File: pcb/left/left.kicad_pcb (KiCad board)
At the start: 2 copper layers, 35.6 x 58.4 mm, 21 parts

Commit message: improve basic design
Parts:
- moved LED3 20.8 mm to (15.2, 27.9), turned to 0 degrees
- moved THUMB1 17.6 mm to (16.5, 66.0)
- moved REF** 15.5 mm to (25.4, 66.0)
- moved REF** 15.2 mm to (0.00, 66.0)
- moved PullR1 14.2 mm to (5.08, 53.3)
- moved PullR2 14.2 mm to (8.89, 53.3)
- moved PullR3 14.0 mm to (12.7, 41.9)
- moved LED2 13.7 mm to (10.2, 27.9), turned to 0 degrees
- moved LEDR3 13.7 mm to (15.2, 31.8)
- moved RST_SW1 13.0 mm to (26.7, 36.1)
- moved RJ45 13.0 mm to (15.2, 55.9)
- moved SIDE1 10.2 mm to (16.5, 61.0)
- moved LEDR2 7.41 mm to (10.2, 31.8), turned to 270 degrees
- moved LED1 6.84 mm to (5.08, 27.9), turned to 0 degrees
- moved REF** 2.54 mm to (25.4, 0.00)
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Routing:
- net GND: track 0.00 -> 21.7 mm
- net +5V: track 0.00 -> 2.54 mm
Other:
- board size 35.6 x 58.4 mm -> 33 x 73.7 mm

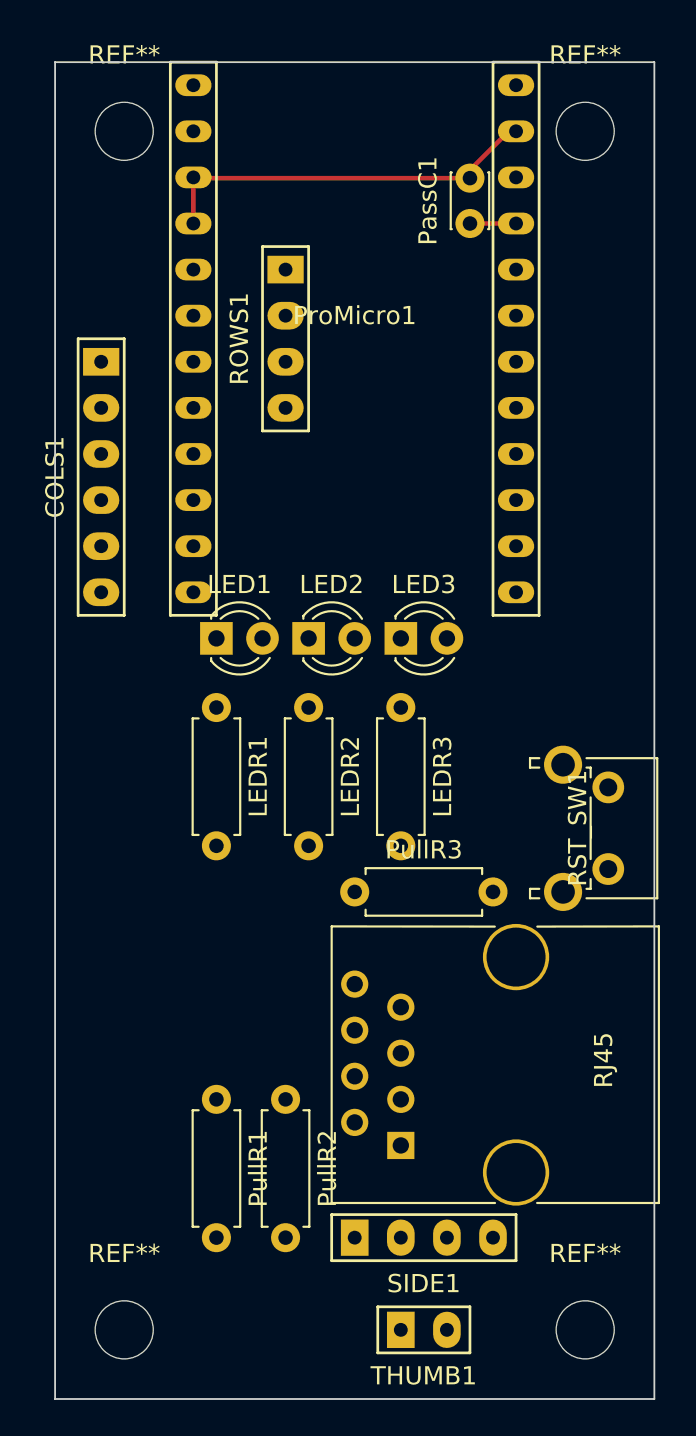
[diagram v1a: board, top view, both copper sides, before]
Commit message: resize pcb shorten pcb length a bit.
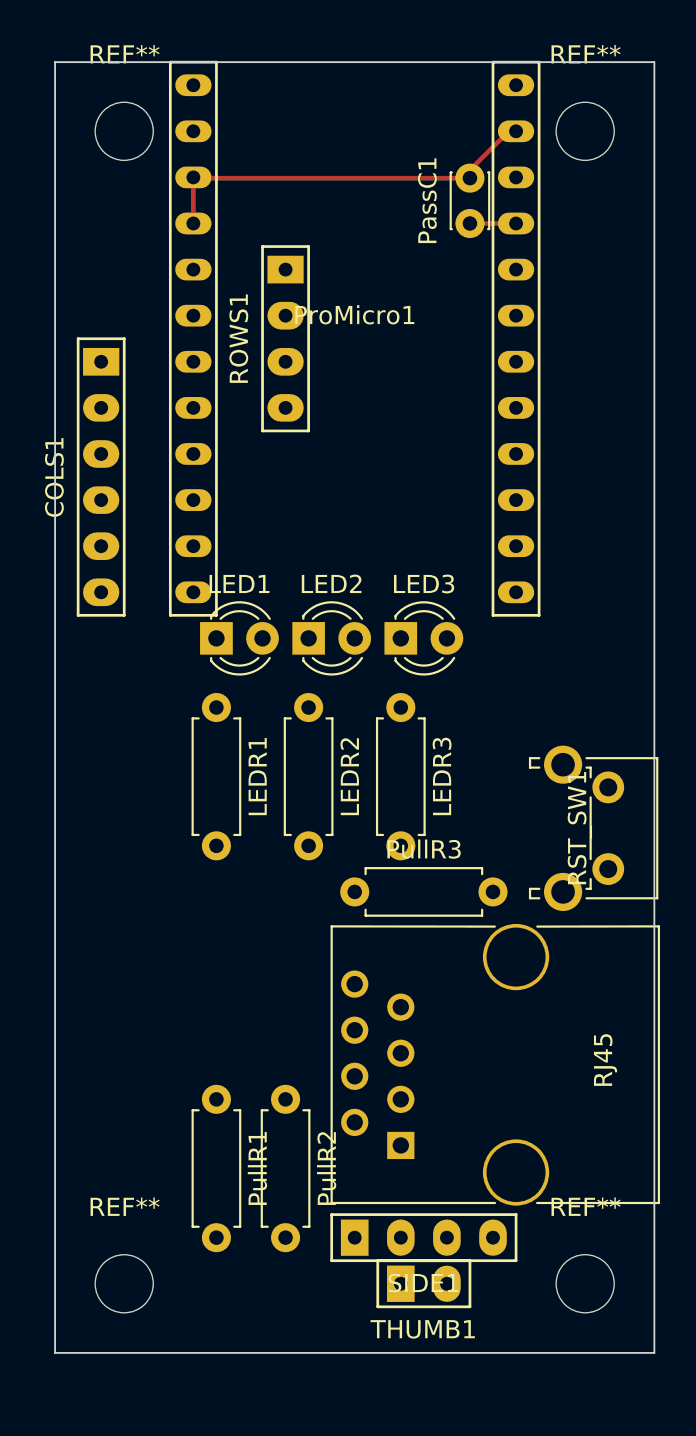
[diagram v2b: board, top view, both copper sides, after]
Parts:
- moved REF** 2.54 mm to (0.00, 63.5)
- moved REF** 2.54 mm to (25.4, 63.5)
- moved THUMB1 2.54 mm to (16.5, 63.5)
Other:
- board size 33 x 73.7 mm -> 33 x 71.1 mm
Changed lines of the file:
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@@
   (general
     (links 45)
-    (no_connects 45)
-    (area -8.290143 -5.178 36.230143 56.958)
+    (no_connects 41)
+    (area -9.560143 -5.178 34.960143 72.198)
     (thickness 1.6)
     (drawings 4)
@@
   )
   (module 4x6t2:Wirepad_01x02 (layer F.Cu)
-    (at 16.51 66.04 90)
+    (at 16.51 63.5 90)
     (fp_text reference THUMB1 (at -2.54 0 180) (layer F.SilkS)
       (effects (font (size 1 1) (thickness 0.15)))
@@
   )
   (module Mounting_Holes:MountingHole_3.2mm_M3 (layer F.Cu)
-    (at 0 66.04)
+    (at 0 63.5)
     (descr "Mounting Hole 3.2mm, no annular, M3")
     (tags "mounting hole 3.2mm no annular m3")
@@
   )
   (module Mounting_Holes:MountingHole_3.2mm_M3 (layer F.Cu)
-    (at 25.4 66.04)
+    (at 25.4 63.5)
     (descr "Mounting Hole 3.2mm, no annular, M3")
     (tags "mounting hole 3.2mm no annular m3")
@@
     (pad 1 np_thru_hole circle (at 0 0) (size 3.2 3.2) (drill 3.2) (layers *.Cu *.Mask))
   )
-  (gr_line (start -3.81 69.85) (end -3.81 -3.81) (layer Edge.Cuts) (width 0.1))
-  (gr_line (start 29.21 69.85) (end -3.81 69.85) (layer Edge.Cuts) (width 0.1))
-  (gr_line (start 29.21 -3.81) (end 29.21 69.85) (layer Edge.Cuts) (width 0.1))
+  (gr_line (start -3.81 67.31) (end -3.81 -3.81) (layer Edge.Cuts) (width 0.1))
+  (gr_line (start 29.21 67.31) (end -3.81 67.31) (layer Edge.Cuts) (width 0.1))
+  (gr_line (start 29.21 -3.81) (end 29.21 67.31) (layer Edge.Cuts) (width 0.1))
   (gr_line (start -3.81 -3.81) (end 29.21 -3.81) (layer Edge.Cuts) (width 0.1))
   (segment (start 3.81 5.08) (end 3.81 2.54) (width 0.25) (layer F.Cu) (net 13))

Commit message: wiring left
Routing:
- net GND: track 21.7 -> 130.2 mm
- net /RST: track 0.00 -> 66.7 mm, vias 0 -> 2
- net +5V: track 2.54 -> 65.7 mm, vias 0 -> 2
- net /SDA: track 0.00 -> 59.5 mm
- net /X: track 0.00 -> 54.8 mm
- net /SCL: track 0.00 -> 51.3 mm
- net /Y: track 0.00 -> 49.8 mm
- net /Thumb_key: track 0.00 -> 40.7 mm, vias 0 -> 1
- net /LED1: track 0.00 -> 18.2 mm
- net /COL0: track 0.00 -> 17.6 mm
- net /COL1: track 0.00 -> 17.5 mm
- net /ROW3: track 0.00 -> 12.7 mm
- net /ROW2: track 0.00 -> 12.7 mm
- net /ROW1: track 0.00 -> 12.7 mm
- net /ROW0: track 0.00 -> 12.7 mm
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- added copper zone on B.Cu, net GND
- added copper zone on F.Cu, net GND

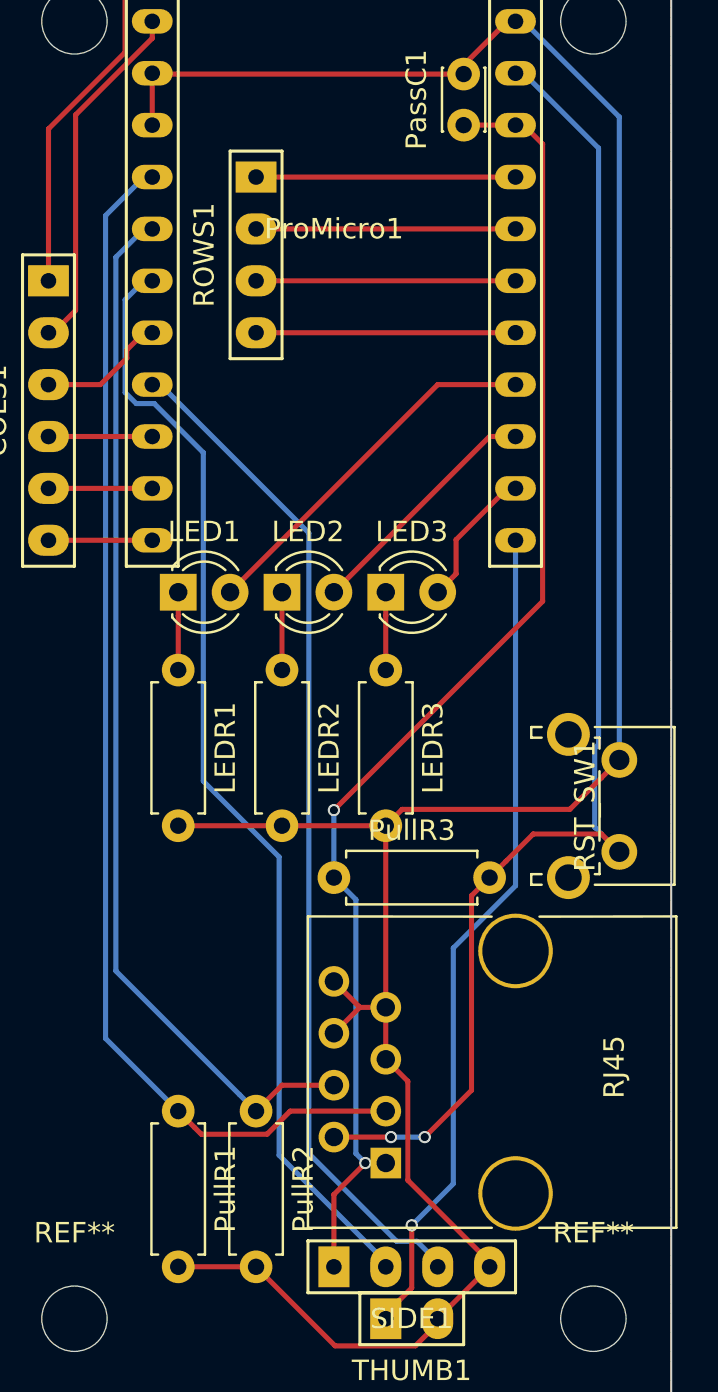
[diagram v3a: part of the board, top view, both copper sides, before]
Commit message: fix LED arrangement LED conflicted with Pro Micro
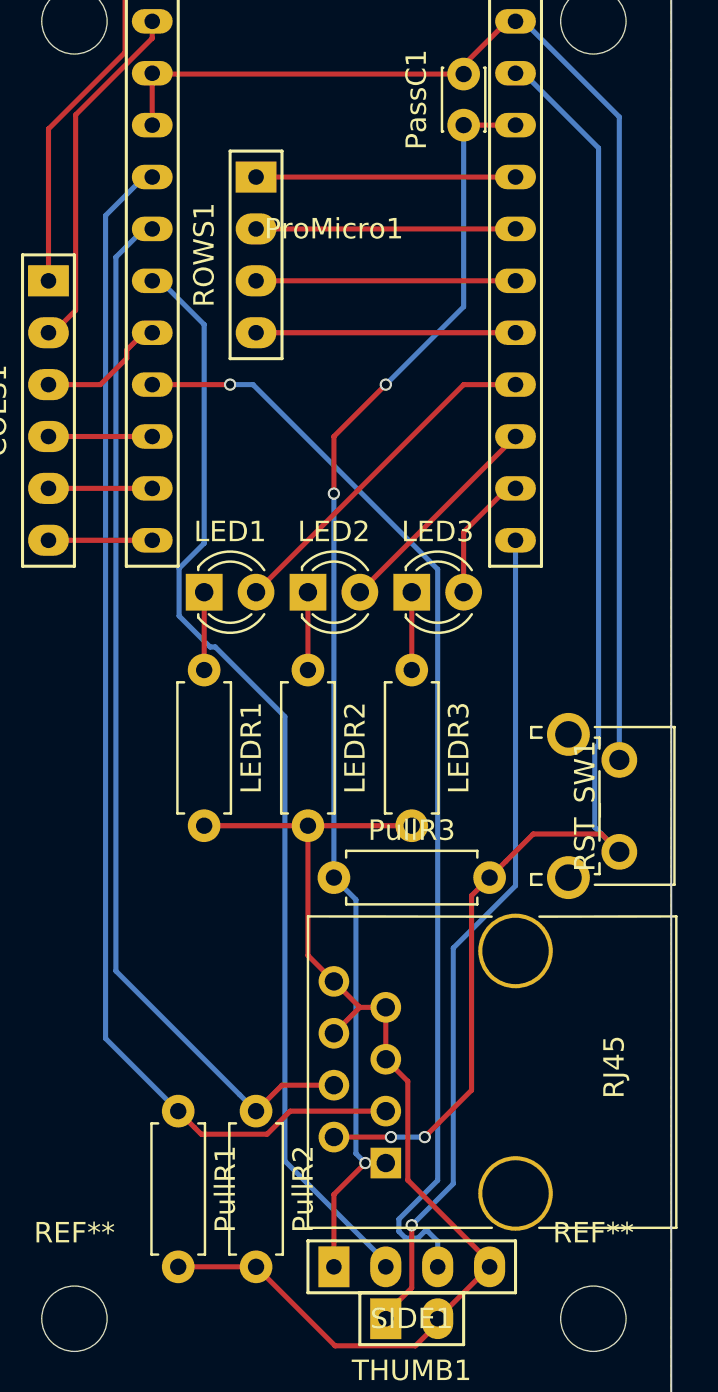
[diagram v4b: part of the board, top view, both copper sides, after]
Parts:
- moved LED3 1.27 mm to (16.5, 27.9)
- moved LEDR3 1.27 mm to (16.5, 31.8)
- moved LED1 1.27 mm to (6.35, 27.9)
- moved LED2 1.27 mm to (11.4, 27.9)
- moved LEDR1 1.27 mm to (6.35, 31.8)
- moved LEDR2 1.27 mm to (11.4, 31.8)
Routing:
- net GND: track 130.2 -> 116.7 mm
- net /Y: track 49.8 -> 54.8 mm, vias 0 -> 1
- net +5V: track 65.7 -> 63.7 mm, vias 2 -> 3
- net /LED2: track 12.0 -> 10.8 mm
- net /LED1: track 18.2 -> 16.9 mm
- net /LED3: track 6.89 -> 6.37 mm

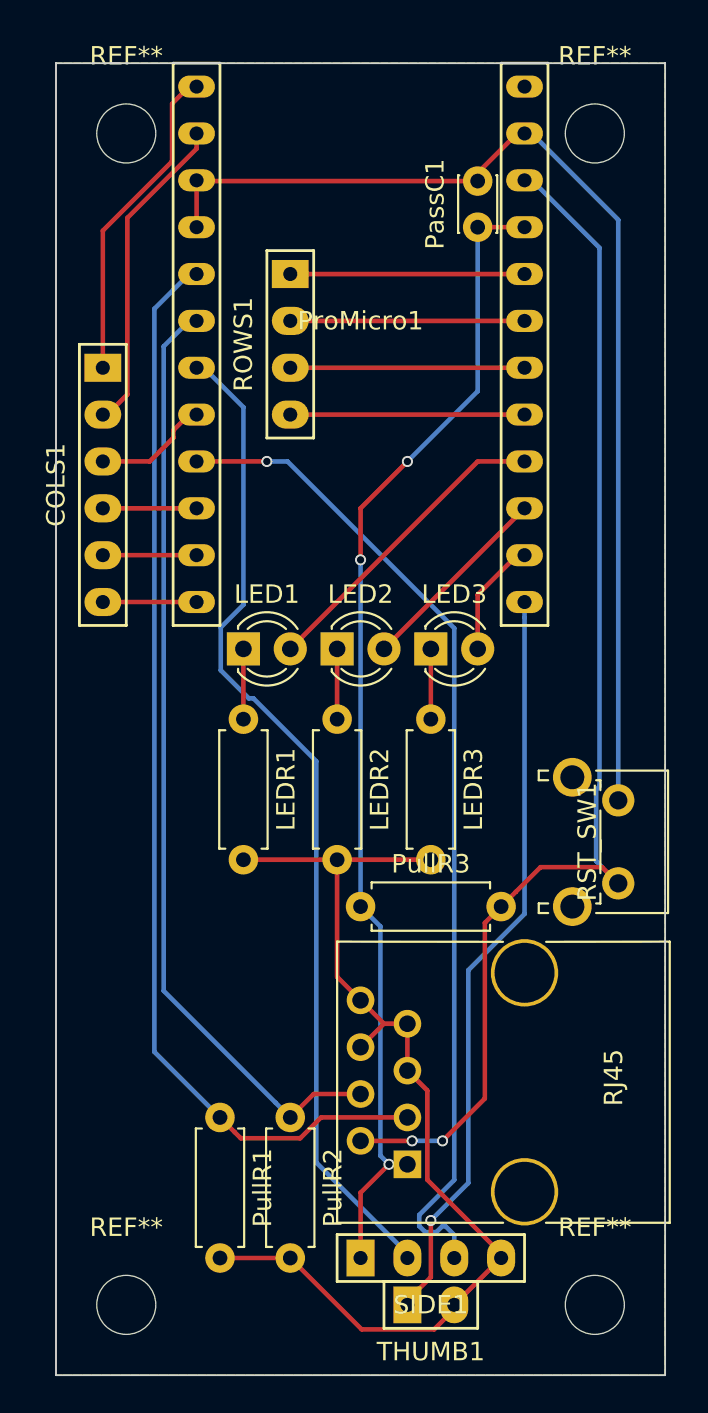
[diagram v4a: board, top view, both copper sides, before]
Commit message: fix pcb size
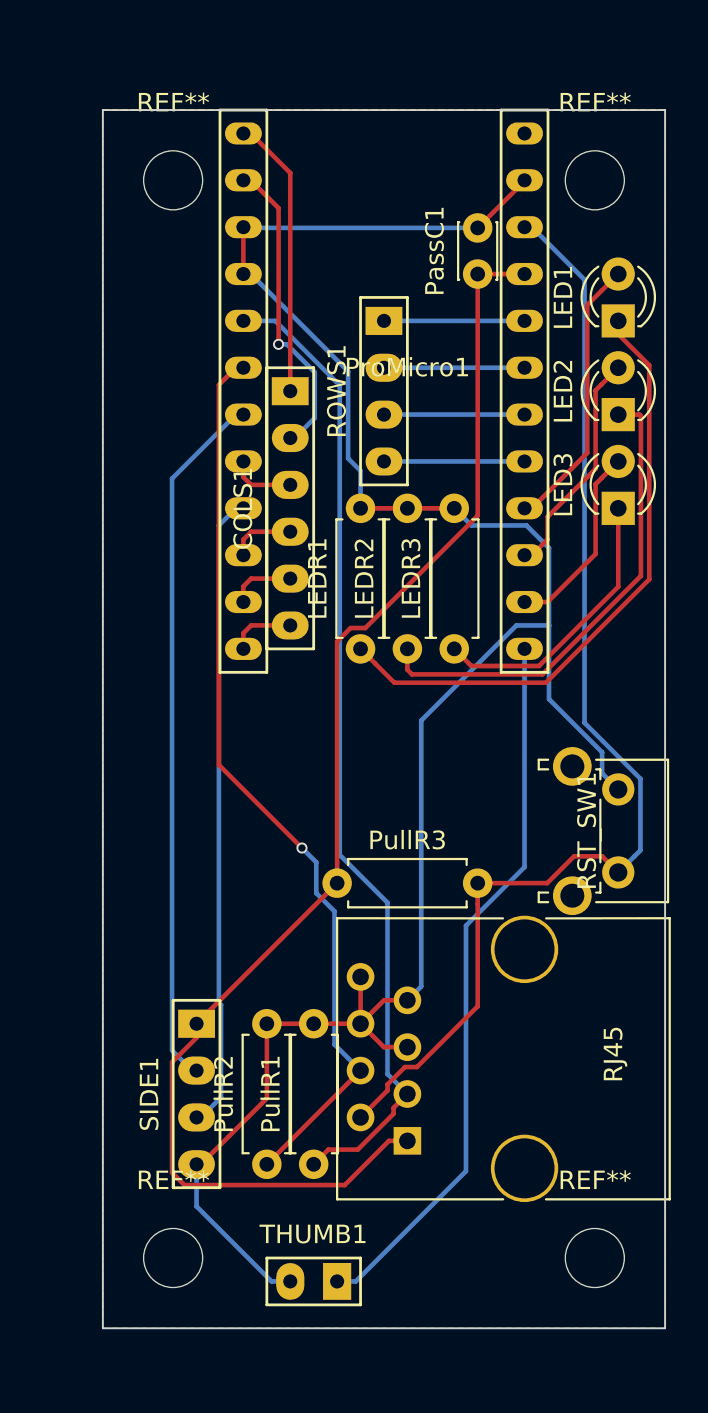
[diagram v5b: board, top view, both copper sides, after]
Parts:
- moved LED1 27.0 mm to (26.7, 10.2), turned to 90 degrees
- moved LED2 19.8 mm to (26.7, 15.2), turned to 90 degrees
- moved SIDE1 15.5 mm to (3.81, 52.1), turned to 0 degrees
- moved LED3 12.7 mm to (26.7, 20.3), turned to 90 degrees
- moved COLS1 10.2 mm to (8.89, 20.3)
- moved LEDR1 7.41 mm to (12.7, 27.9), turned to 90 degrees
- moved THUMB1 6.48 mm to (10.2, 62.2), turned to 270 degrees
- moved ROWS1 5.68 mm to (14.0, 14.0)
- moved PullR1 5.68 mm to (10.2, 55.9), turned to 90 degrees
- moved LEDR2 5.39 mm to (15.2, 27.9), turned to 90 degrees
- moved LEDR3 4.02 mm to (17.8, 27.9), turned to 90 degrees
- moved ProMicro1 3.59 mm to (15.2, 14.0)
- moved REF** 3.59 mm to (2.54, 2.54)
- moved REF** 3.59 mm to (2.54, 61.0)
- moved PullR2 2.84 mm to (7.62, 55.9), turned to 90 degrees
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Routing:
- net Net-(LED1-Pad1): track 3.81 -> 33.4 mm
- net Net-(LED2-Pad1): track 3.81 -> 26.0 mm
- net /Y: track 54.8 -> 34.5 mm, vias 1 -> 0
- net /X: track 54.4 -> 38.1 mm
- net Net-(LED3-Pad1): track 3.81 -> 15.3 mm
- net +5V: track 63.7 -> 72.6 mm, vias 3 -> 0
- net /SDA: track 59.5 -> 53.5 mm
- net /ROW3: track 12.7 -> 7.62 mm
- net /ROW2: track 12.7 -> 7.62 mm
- net /ROW1: track 12.7 -> 7.62 mm
- net /ROW0: track 12.7 -> 7.62 mm
- net /LED3: track 6.37 -> 10.5 mm
- net /RST: track 66.7 -> 62.6 mm, vias 2 -> 0
- net /COL2: track 6.37 -> 3.56 mm
- net /COL0: track 17.6 -> 15.3 mm
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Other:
- board size 33 x 71.1 mm -> 30.5 x 66 mm
